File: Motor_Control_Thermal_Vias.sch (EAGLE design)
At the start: 33 parts, among them J1 63971-1-QC_TAB-RA, J2 63971-1-QC_TAB-RA, J3 63971-1-QC_TAB-RA, J4 63971-1-QC_TAB-RA, Q1 FBDL0120N40-MO-299A, Q2 FBDL0120N40-MO-299A, Q3 FBDL0120N40-MO-299A, Q4 FBDL0120N40-MO-299A, U1 A3941-TSSOP28-LP

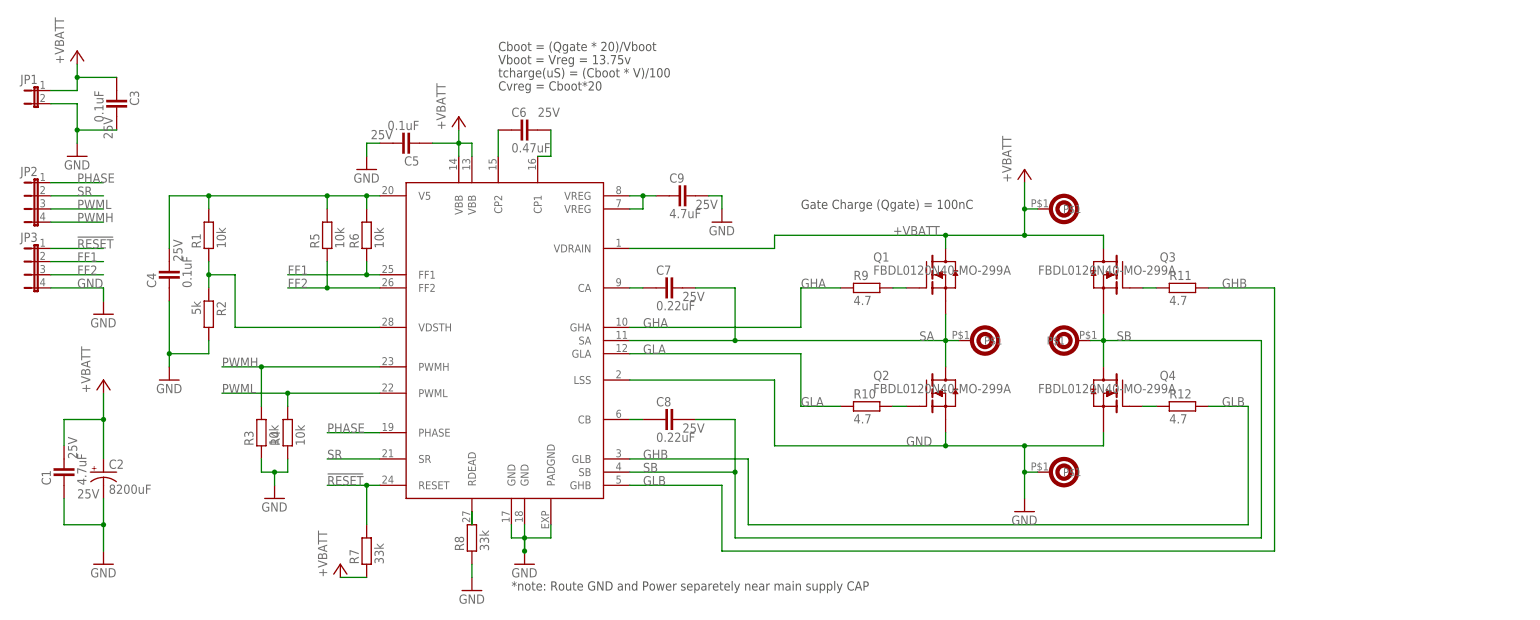
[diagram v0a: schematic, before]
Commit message: More Via's!
It can't be a bad thing to add more via's to improve thermals. I also
added another CAP to improve noise. Silkscreen is updated and the board
is ready for production!
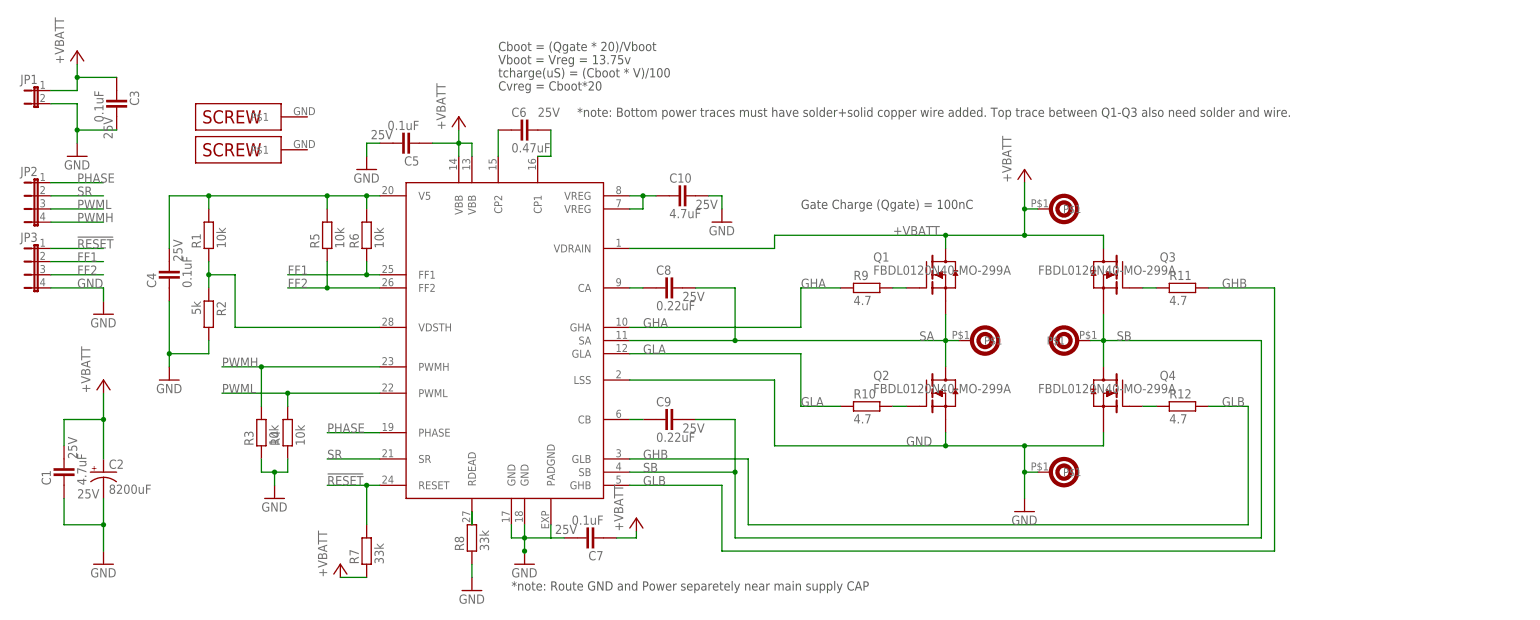
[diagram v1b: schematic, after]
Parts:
- added C10: 4.7uF, Motor_Control:CAPACITOR_0603
- added SCREW1, SCREW2: SCREW-4MM, Motor_Control:SCREW-4MM
- C7: value 0.22uF -> 0.1uF; device Motor_Control:CAPACITOR_0603L -> Motor_Control:CAPACITOR_0603
- C9: value 4.7uF -> 0.22uF; device Motor_Control:CAPACITOR_0603 -> Motor_Control:CAPACITOR_0603L
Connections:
- net +VBATT: now also C7.1
- net GND: now also C10.2, C7.2; no longer C9.2
- net N$15: now also C9.1; no longer C8.1
- net N$5: now also C10.1; no longer C9.1
- net N$6: now also C8.1; no longer C7.1
- net SA: now also C8.2; no longer C7.2
- net SB: now also C9.2; no longer C8.2
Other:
- note added: "*note: Bottom power traces must have solder+solid copper wire added. Top trace between Q1-Q3 also need solder and wire."
- moved on the sheet: C7, C8, C9
